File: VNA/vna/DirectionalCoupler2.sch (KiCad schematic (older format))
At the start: 4 parts, among them T3 Transformer_1P_1S, T4 Transformer_1P_1S

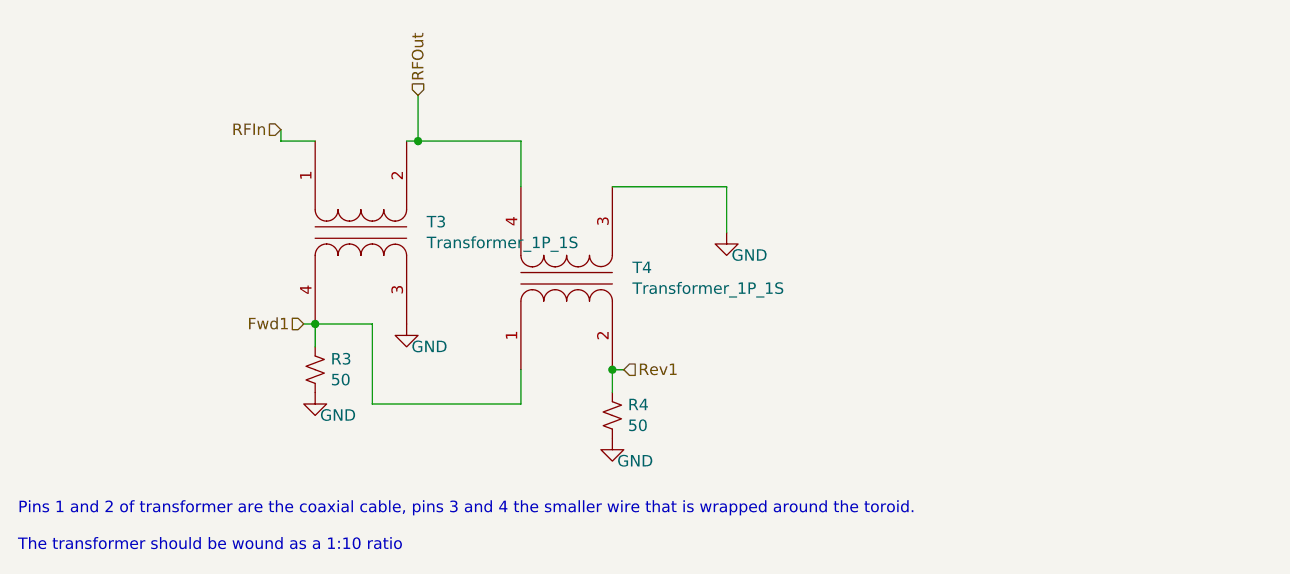
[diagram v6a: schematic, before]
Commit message: custom footprint for couplers, added decoupling caps
added custom footprint for directional couplers - will need to verify it

added decoupling caps to ad9851
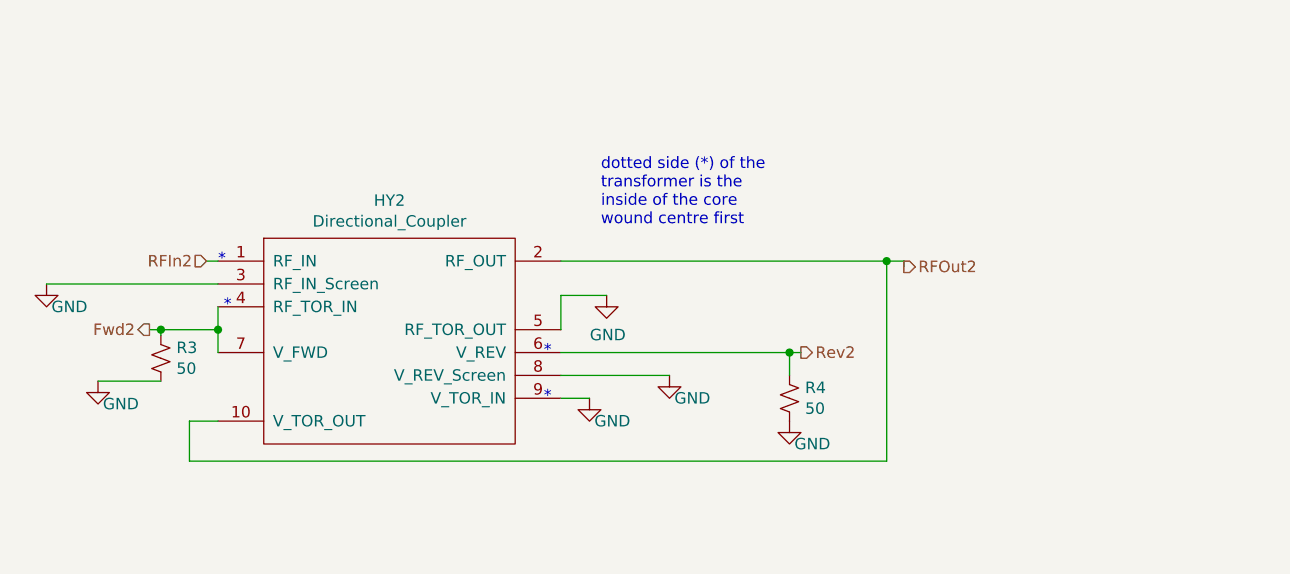
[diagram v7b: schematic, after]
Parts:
- removed T3, T4: Transformer_1P_1S, symbol Device:Transformer_1P_1S
- added HY2: Directional_Coupler, vna:Directional_Coupler, symbol vna-rescue:Directional_Coupler
- R3, R4: footprint Resistor_SMD:R_0805_2012Metric_Pad1.15x1.40mm_HandSolder -> Resistor_SMD:R_1206_3216Metric_Pad1.42x1.75mm_HandSolder
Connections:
- net GND: now also HY2.3 (RF_IN_Screen), HY2.5 (RF_TOR_OUT), HY2.8 (V_REV_Screen), HY2.9 (V_TOR_IN)
- net Fwd1 renamed Fwd2
- net Fwd2: now also HY2.4 (RF_TOR_IN), HY2.7 (V_FWD)
- net Rev1 renamed Rev2
- net Rev2: now also HY2.6 (V_REV)
- new net RFIn2: HY2.1 (RF_IN)
- new net RFOut2: HY2.10 (V_TOR_OUT), HY2.2 (RF_OUT)
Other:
- note added: "*"
- note added: "dotted side (*) of the \ntransformer is the \ninside of the core\nwound centre first"
- note removed: "Pins 1 and 2 of transformer are the coaxial cable, pins 3 and 4 the smaller wire that is wrapped around the toroid.\n\nThe transformer should be wound as a 1:10 ratio"

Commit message: initial pcb design
initial layout and grouping of components complete
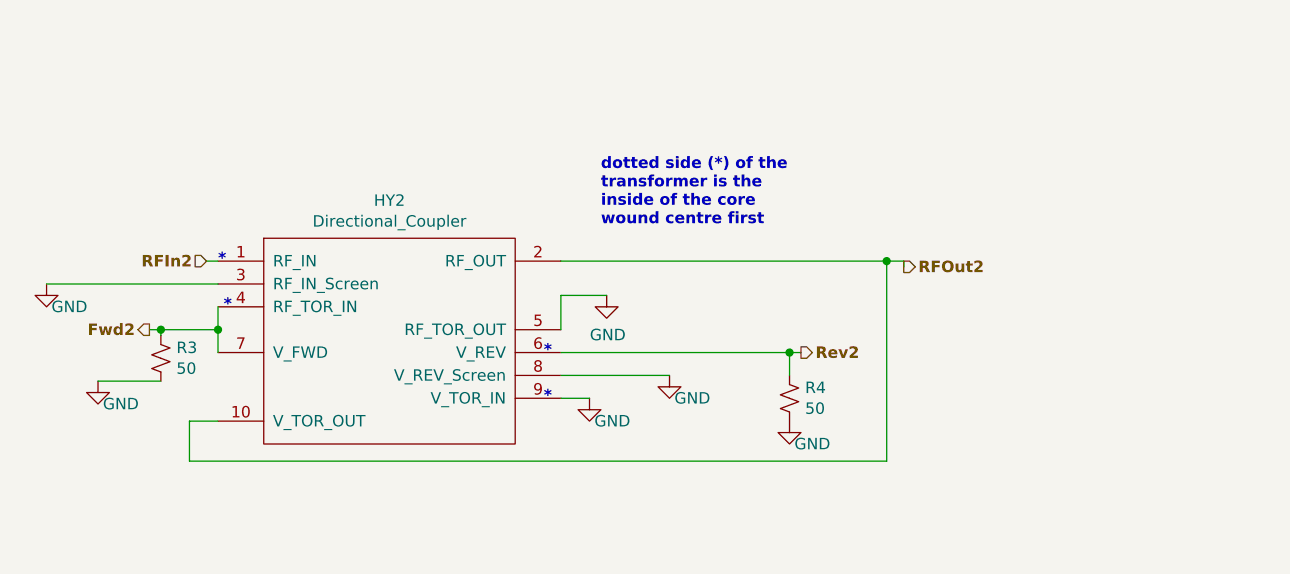
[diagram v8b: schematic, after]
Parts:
- R3, R4: footprint Resistor_SMD:R_1206_3216Metric_Pad1.42x1.75mm_HandSolder -> Resistor_SMD:R_0805_2012Metric_Pad1.15x1.40mm_HandSolder
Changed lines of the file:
@@
 encoding utf-8
 Sheet 10 10
-Title ""
-Date ""
-Rev ""
-Comp ""
+Title "Directional Coupler 2"
+Date "2019-09-25"
+Rev "0.1"
+Comp "Benjamin Jackson"
 Comment1 ""
 Comment2 ""
@@
 F 0 "R4" H 7043 4121 50  0000 L CNN
 F 1 "50" H 7043 4030 50  0000 L CNN
-F 2 "Resistor_SMD:R_1206_3216Metric_Pad1.42x1.75mm_HandSolder" H 6975 4075 50  0001 C CNN
+F 2 "Resistor_SMD:R_0805_2012Metric_Pad1.15x1.40mm_HandSolder" H 6975 4075 50  0001 C CNN
 F 3 "~" H 6975 4075 50  0001 C CNN
 	1    6975 4075
@@
 F 0 "R3" H 4293 3946 50  0000 L CNN
 F 1 "50" H 4293 3855 50  0000 L CNN
-F 2 "Resistor_SMD:R_1206_3216Metric_Pad1.42x1.75mm_HandSolder" H 4225 3900 50  0001 C CNN
+F 2 "Resistor_SMD:R_0805_2012Metric_Pad1.15x1.40mm_HandSolder" H 4225 3900 50  0001 C CNN
 F 3 "~" H 4225 3900 50  0001 C CNN
 	1    4225 3900
@@
 	1    0    0    -1
 $EndComp
-Text HLabel 4175 3775 0    50   Output ~ 0
+Text HLabel 4175 3775 0    50   Output ~ 10
 Fwd2
-Text HLabel 7025 3875 2    50   Output ~ 0
+Text HLabel 7025 3875 2    50   Output ~ 10
 Rev2
-Text HLabel 7475 3500 2    50   Output ~ 0
+Text HLabel 7475 3500 2    50   Output ~ 10
 RFOut2
-Text HLabel 4425 3475 0    50   Input ~ 0
+Text HLabel 4425 3475 0    50   Input ~ 10
 RFIn2
 $Comp
@@
 Wire Wire Line
 	5975 3975 6450 3975
-Text Notes 6150 3325 0    50   ~ 0
+Text Notes 6150 3325 0    50   ~ 10
 dotted side (*) of the \ntransformer is the \ninside of the core\nwound centre first
 Wire Wire Line
@@
 Wire Wire Line
 	4350 4350 7400 4350
-Text Notes 4475 3500 0    50   ~ 0
-*
-Text Notes 4500 3700 0    50   ~ 0
-*
-Text Notes 5900 3900 0    50   ~ 0
-*
-Text Notes 5900 4100 0    50   ~ 0
+Text Notes 4475 3500 0    50   ~ 10
+*
+Text Notes 4500 3700 0    50   ~ 10
+*
+Text Notes 5900 3900 0    50   ~ 10
+*
+Text Notes 5900 4100 0    50   ~ 10
 *
 $EndSCHEMATC
